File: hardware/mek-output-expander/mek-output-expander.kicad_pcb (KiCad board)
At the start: 2 copper layers, 150 x 80 mm, 133 parts, among them J2 TC2030, J4 Screw_Terminal_01x02, J5 Screw_Terminal_01x02, J6 Screw_Terminal_01x02, J7 Screw_Terminal_01x02, J8 Screw_Terminal_01x02, Q1 BT136S-800E, Q2 BT136S-800E, Q3 BT136S-800E, Q4 BT136S-800E, Q5 BT136S-800E, Q6 BT136S-800E, Q7 BT136S-800E, Q8 BT136S-800E, U1 LMR38020FDDAR, U10 MOC3063S, U11 MOC3063S, U12 MOC3063S, U13 MOC3063S, U14 MOC3063S, U2 AMS1117-3.3, U3 24C02, U4 CH32V003FxPx, U5 SN65HVD72DR, U6 ULN2803A, U7 MOC3063S, U8 MOC3063S, U9 MOC3063S, Y1 24Mhz

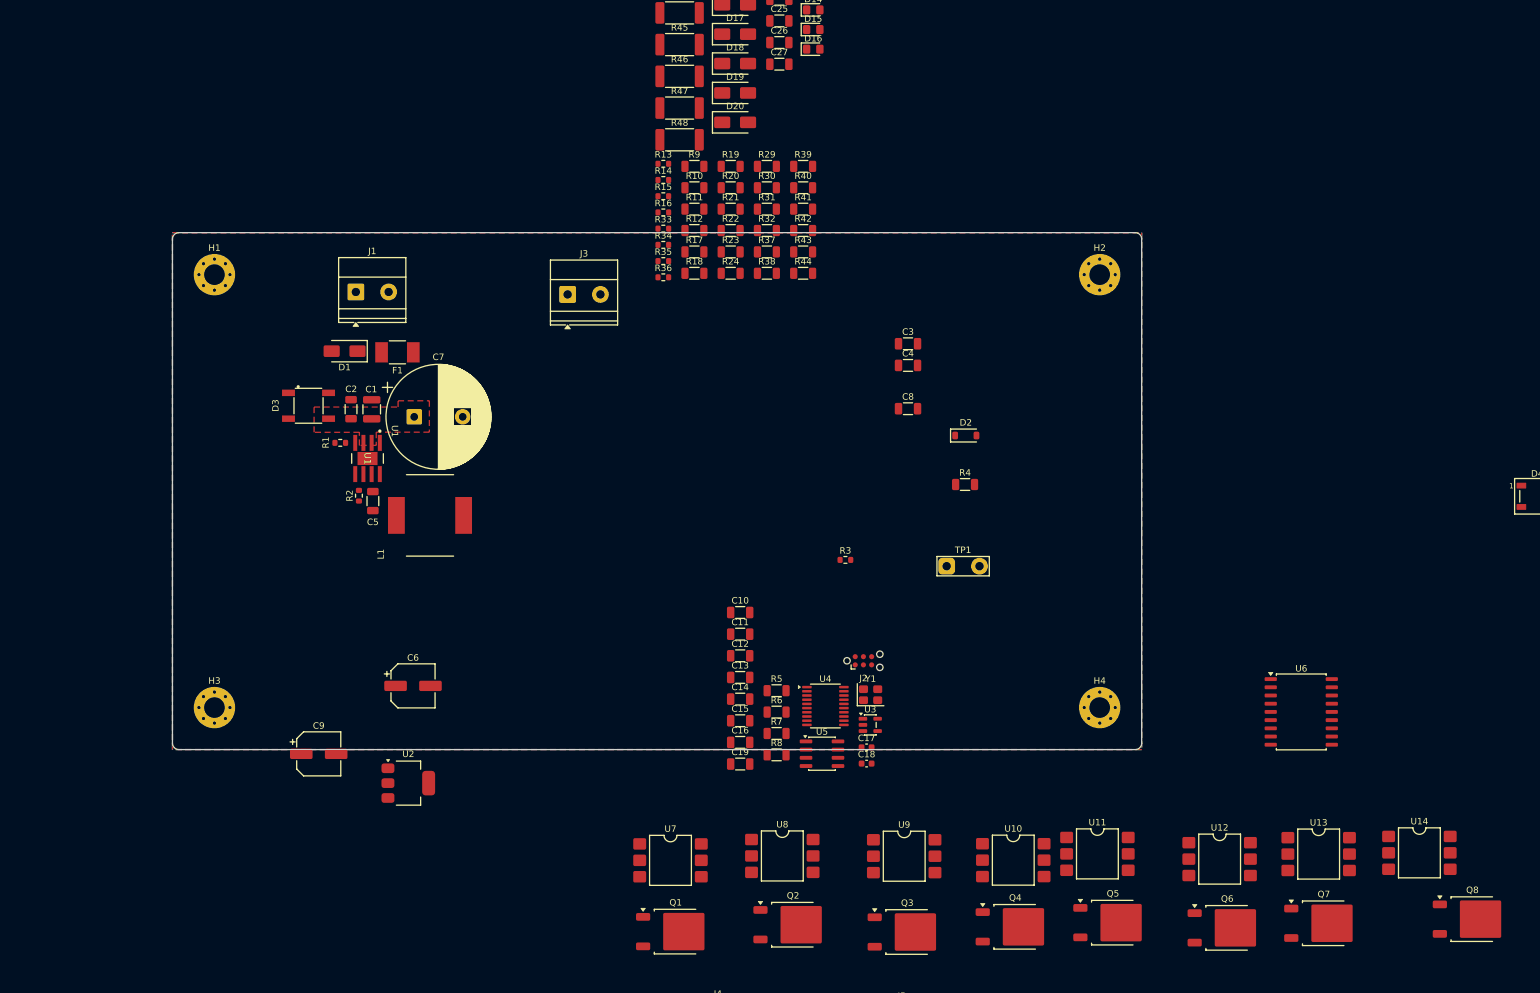
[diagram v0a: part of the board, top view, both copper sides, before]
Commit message: Update bridge rectifier 3d model
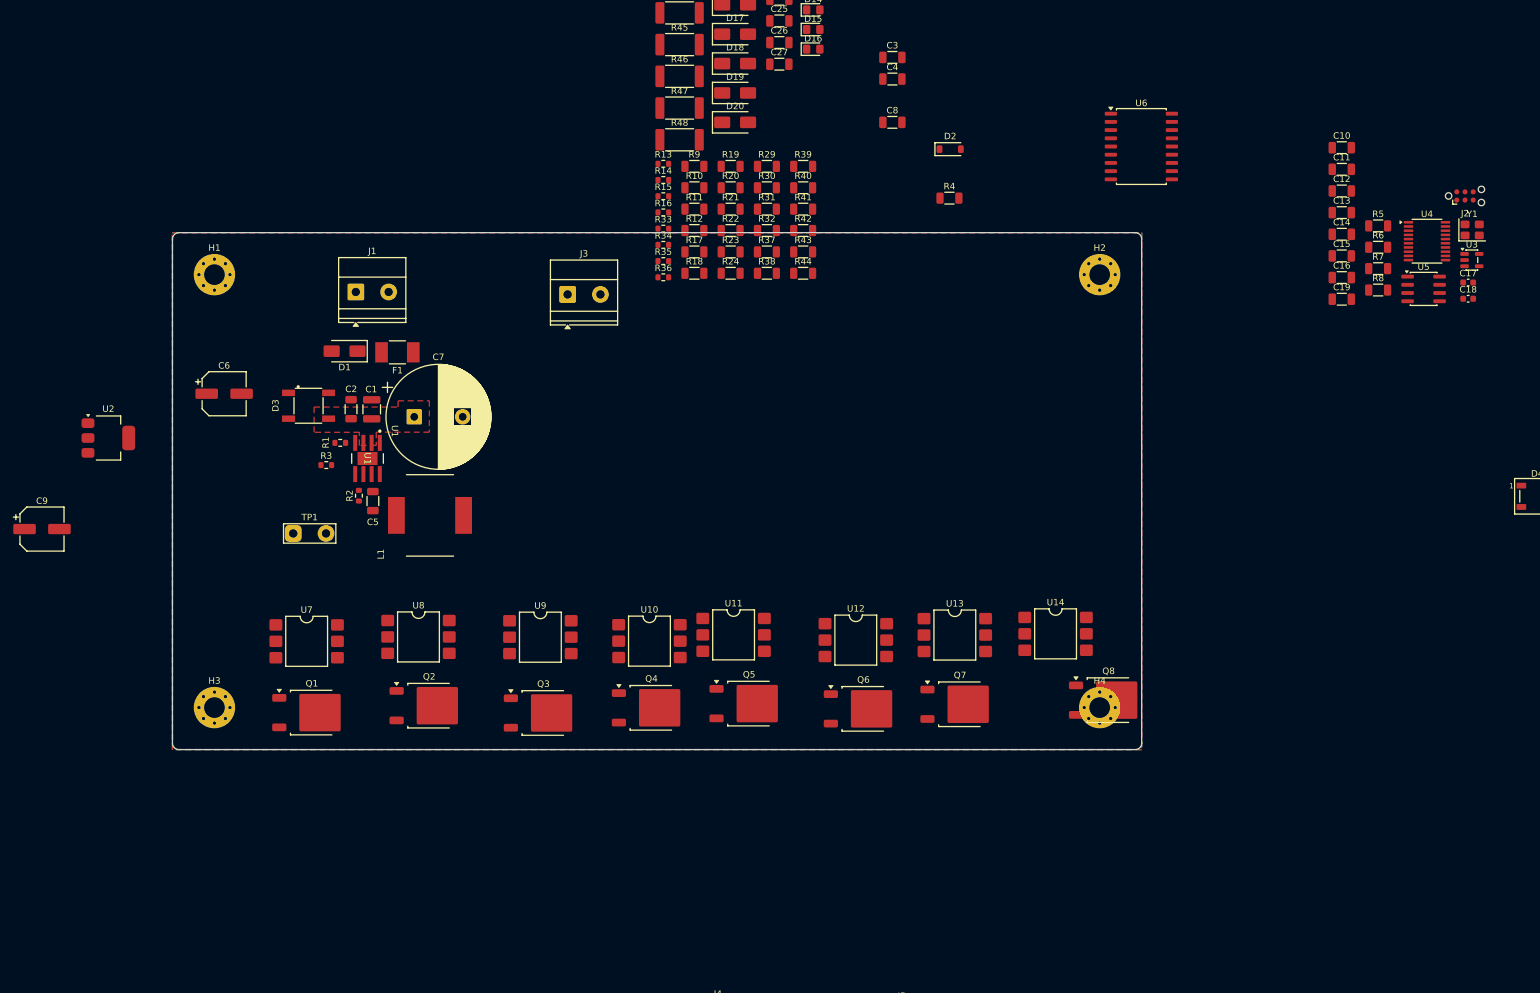
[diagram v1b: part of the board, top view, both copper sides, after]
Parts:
- moved J2 117.7 mm to (270.0, 34.3)
- moved R5 117.7 mm to (256.6, 39.0)
- moved R6 117.7 mm to (256.6, 42.3)
- moved R7 117.7 mm to (256.6, 45.6)
- moved R8 117.7 mm to (256.6, 48.9)
- moved U3 117.7 mm to (271.1, 44.2)
- moved C10 117.7 mm to (251.0, 26.9)
- moved C11 117.7 mm to (251.0, 30.2)
- moved C12 117.7 mm to (251.0, 33.5)
- moved C13 117.7 mm to (251.0, 36.9)
- moved C14 117.7 mm to (251.0, 40.2)
- moved C15 117.7 mm to (251.0, 43.6)
- moved C16 117.7 mm to (251.0, 47.0)
- moved C19 117.7 mm to (251.0, 50.3)
- moved U5 117.7 mm to (263.6, 48.7)
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
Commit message: Board, scripts and 3d model updates
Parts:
- removed TP1: TestPoint_2Pole, TestPoint:TestPoint_2Pads_Pitch5.08mm_Drill1.3mm
- U6: footprint Package_SO:SOP-18_7.495x11.515mm_P1.27mm -> Package_SO:SOIC-18W_7.5x11.6mm_P1.27mm
- moved D9 136.1 mm to (79.5, 103.0)
- moved C20 128.9 mm to (84.5, 92.0), turned to 90 degrees
- moved D5 126.1 mm to (78.5, 78.0), turned to 90 degrees
- moved R25 124.8 mm to (85.5, 99.0), turned to -90 degrees
- moved D10 122.7 mm to (97.5, 103.0)
- moved C21 115.7 mm to (102.5, 92.0), turned to 90 degrees
- moved R26 112.2 mm to (103.5, 99.0), turned to -90 degrees
- moved D6 111.5 mm to (96.5, 78.0), turned to 90 degrees
- moved D11 110.8 mm to (115.5, 103.0)
- moved J2 110.8 mm to (163.0, 63.0)
- moved C22 104.2 mm to (120.5, 92.0), turned to 90 degrees
- moved R27 101.5 mm to (121.5, 99.0), turned to -90 degrees
- moved D12 101.0 mm to (133.6, 103.0)
- moved D7 98.1 mm to (114.5, 78.0), turned to 90 degrees
- moved R48 96.8 mm to (211.7, 99.0), turned to -90 degrees
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
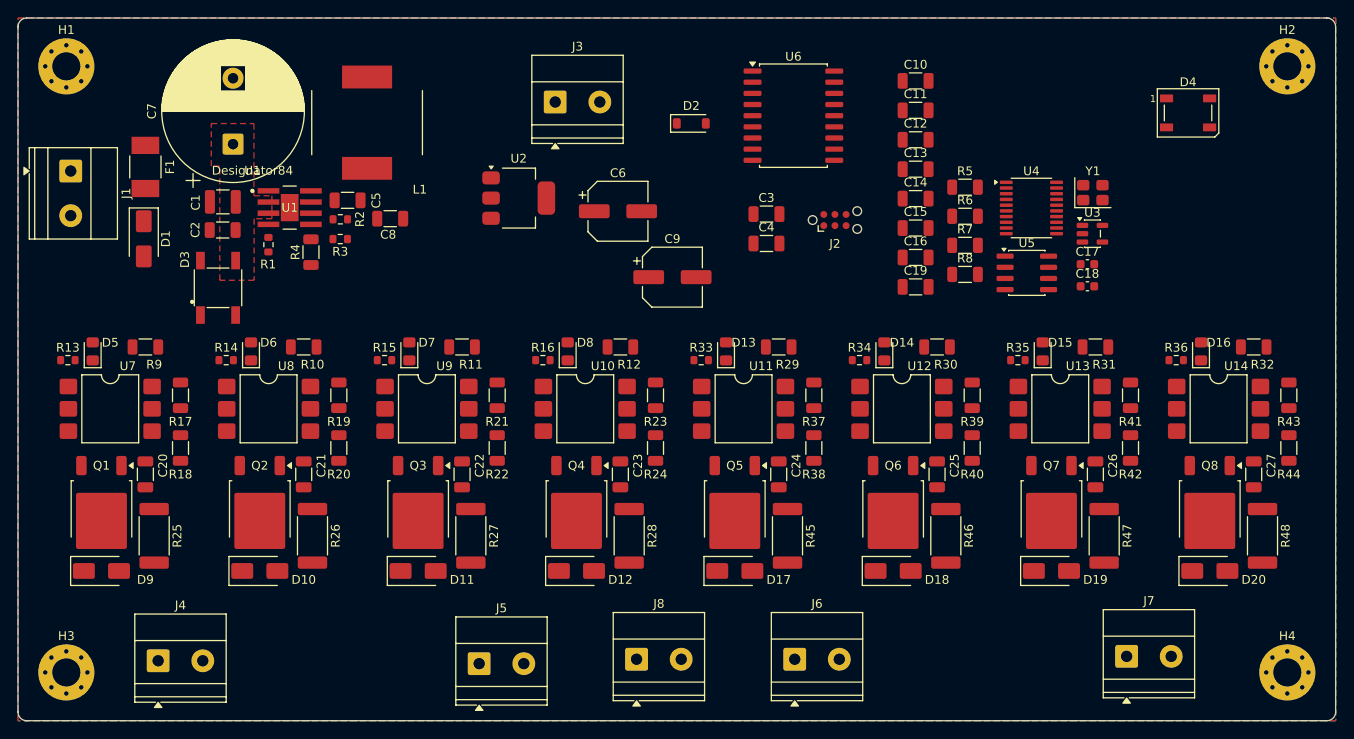
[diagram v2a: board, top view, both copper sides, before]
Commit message: Configure net classes + board stack up changes for edge script
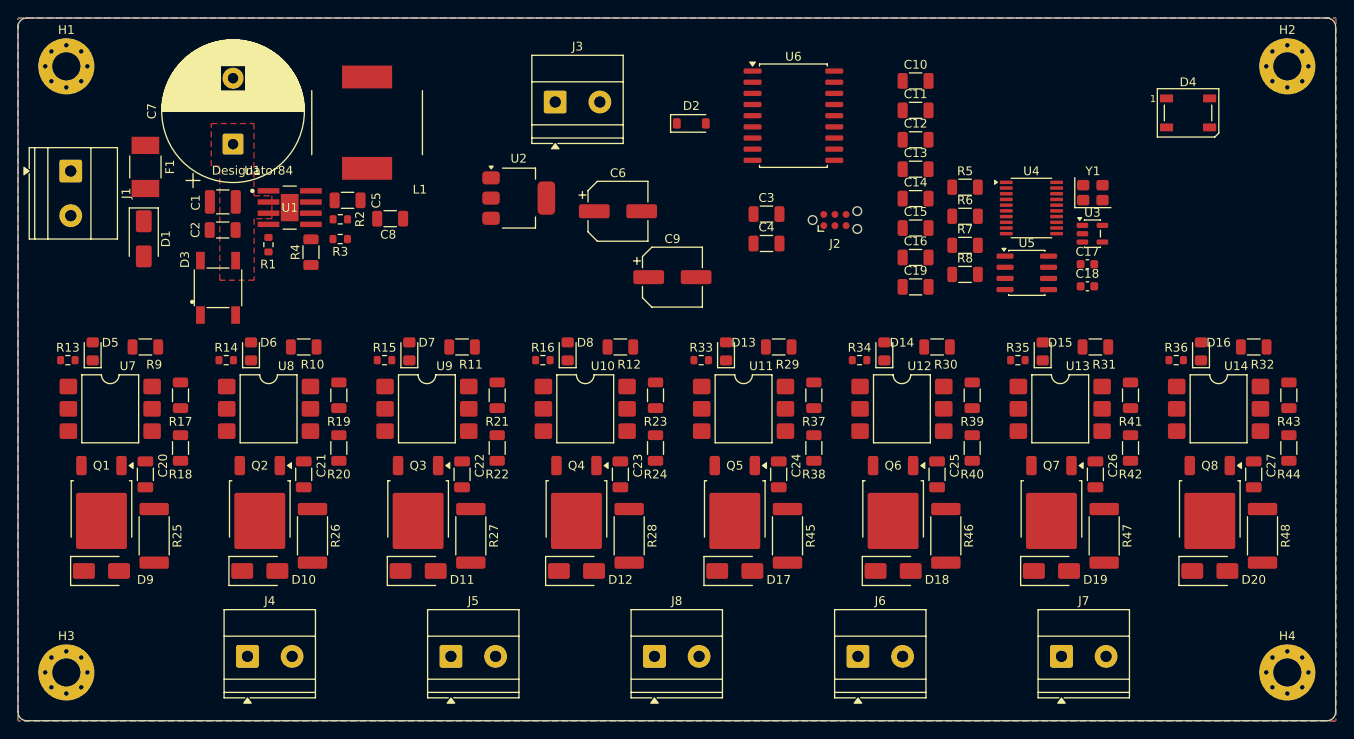
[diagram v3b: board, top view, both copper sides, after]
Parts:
- moved J4 10.2 mm to (96.1, 112.7)
- moved J7 7.42 mm to (188.8, 112.7)
- moved J6 7.21 mm to (165.6, 112.7)
- moved J5 3.32 mm to (119.3, 112.7)
- moved J8 2.06 mm to (142.5, 112.7)
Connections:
- J4 pad 1: OP2_MT1 -> OP1_MT1
- J4 pad 2: OP1_MT1 -> OP2_MT1
- J5 pad 1: OP4_MT1 -> OP3_MT1
- J5 pad 2: OP3_MT1 -> OP4_MT1
- J6 pad 1: OP6_MT1 -> OP5_MT1
- J6 pad 2: OP5_MT1 -> OP6_MT1
- J7 pad 1: OP8_MT1 -> OP7_MT1
- J7 pad 2: OP7_MT1 -> OP8_MT1
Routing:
- added copper zone on In2.Cu, net 24VAC_COM
- added copper zone on B.Cu, net 24VAC_PWR_FUSED
- added copper zone on In1.Cu, net GND
- added copper zone on In2.Cu, net GND
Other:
- copper layers 2 -> 4

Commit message: Updates
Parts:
- moved F1 14.8 mm to (77.0, 69.8)
- moved R43 4.54 mm to (213.4, 78.6)
- moved R41 4.47 mm to (195.6, 78.6)
- moved R39 4.41 mm to (177.9, 78.6)
- moved R17 4.41 mm to (89.2, 78.6)
- moved R37 4.37 mm to (160.2, 78.6)
- moved R19 4.37 mm to (106.9, 78.6)
- moved R23 4.35 mm to (142.4, 78.6)
- moved R21 4.35 mm to (124.7, 78.6)
- moved R13 2.84 mm to (78.5, 79.4)
- moved D5 2.79 mm to (81.3, 78.2), turned to -90 degrees
- moved R14 2.56 mm to (96.2, 79.4)
- moved D6 2.51 mm to (99.0, 78.2), turned to -90 degrees
- moved R15 2.28 mm to (114.0, 79.4)
- moved D7 2.22 mm to (116.8, 78.2), turned to -90 degrees
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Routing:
- net 24VAC_PWR_FUSED: track 0.00 -> 128.4 mm, vias 0 -> 57
- net +5V: track 0.00 -> 96.7 mm
- net OP1_MT1: track 0.00 -> 41.0 mm
- net OP8_MT1: track 0.00 -> 20.2 mm
- net OP6_MT1: track 0.00 -> 20.2 mm
- net OP5_MT1: track 0.00 -> 20.2 mm
- net OP2_MT1: track 0.00 -> 20.2 mm
- net OP4_MT1: track 0.00 -> 20.2 mm
- net OP7_MT1: track 0.00 -> 20.2 mm
- net OP3_MT1: track 0.00 -> 20.2 mm
- net Net-(Q7-G): track 0.00 -> 13.1 mm
- net Net-(Q6-G): track 0.00 -> 13.1 mm
- net Net-(Q4-G): track 0.00 -> 13.1 mm
- net Net-(Q2-G): track 0.00 -> 13.1 mm
- net Net-(Q1-G): track 0.00 -> 13.1 mm
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- added copper zone on F.Cu, net 24VAC_COM
- added copper zone on B.Cu, net 24VAC_PWR
- added copper zone on F.Cu, net 24VAC_PWR
- added copper zone on F.Cu, net 24VAC_PWR_FUSED

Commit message: Script fix
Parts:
- moved C22 0.27 mm to (121.1, 92.0)
- moved C23 0.27 mm to (138.8, 92.0)
- moved C24 0.27 mm to (156.6, 92.0)
- moved C26 0.27 mm to (192.1, 92.0)
- moved C27 0.27 mm to (209.8, 92.0)
- moved R27 0.27 mm to (122.1, 99.0)
- moved R28 0.27 mm to (139.8, 99.0)
- moved R45 0.27 mm to (157.6, 99.0)
- moved R47 0.27 mm to (193.1, 99.0)
- moved R48 0.27 mm to (210.8, 99.0)
- moved C20 0.27 mm to (85.6, 92.0)
- moved C21 0.27 mm to (103.4, 92.0)
- moved R25 0.27 mm to (86.6, 99.0)
- moved R26 0.27 mm to (104.4, 99.0)
- moved C25 0.27 mm to (174.3, 92.0)
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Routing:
- net 24VAC_PWR_FUSED: track 128.4 -> 161.2 mm, vias 57 -> 91
- net GND: track 0.00 -> 1.73 mm, vias 0 -> 6
- added copper zone on F.Cu, net OP1_MT1
